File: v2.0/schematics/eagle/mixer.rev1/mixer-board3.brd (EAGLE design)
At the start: 100 x 80 mm, 64 parts, among them IC1 TL082P, IC2 TL082P, IC3 TL082P, IC4 TL082P, J1 RTN-2, J2 RTN-1, J3 SEND1, J4 SEND2

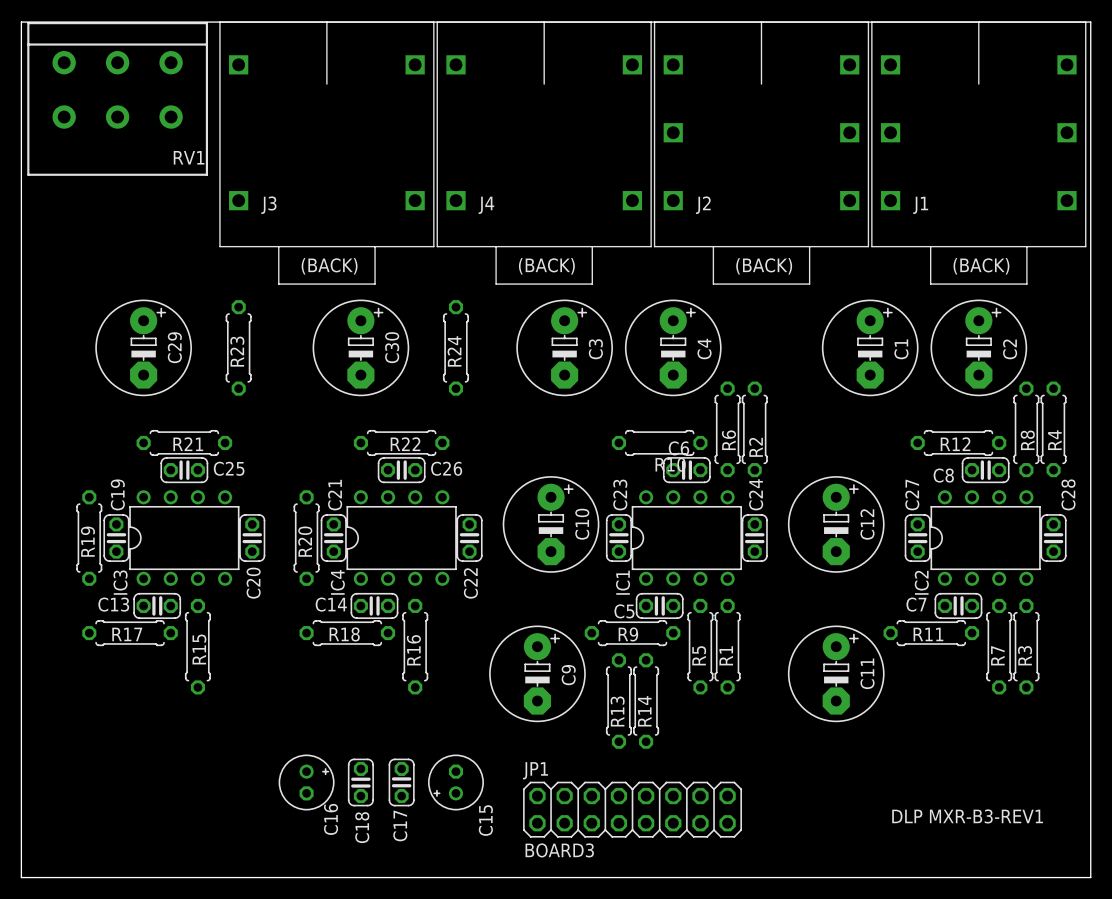
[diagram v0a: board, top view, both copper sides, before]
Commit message: Mixer board 3 route and ground plane
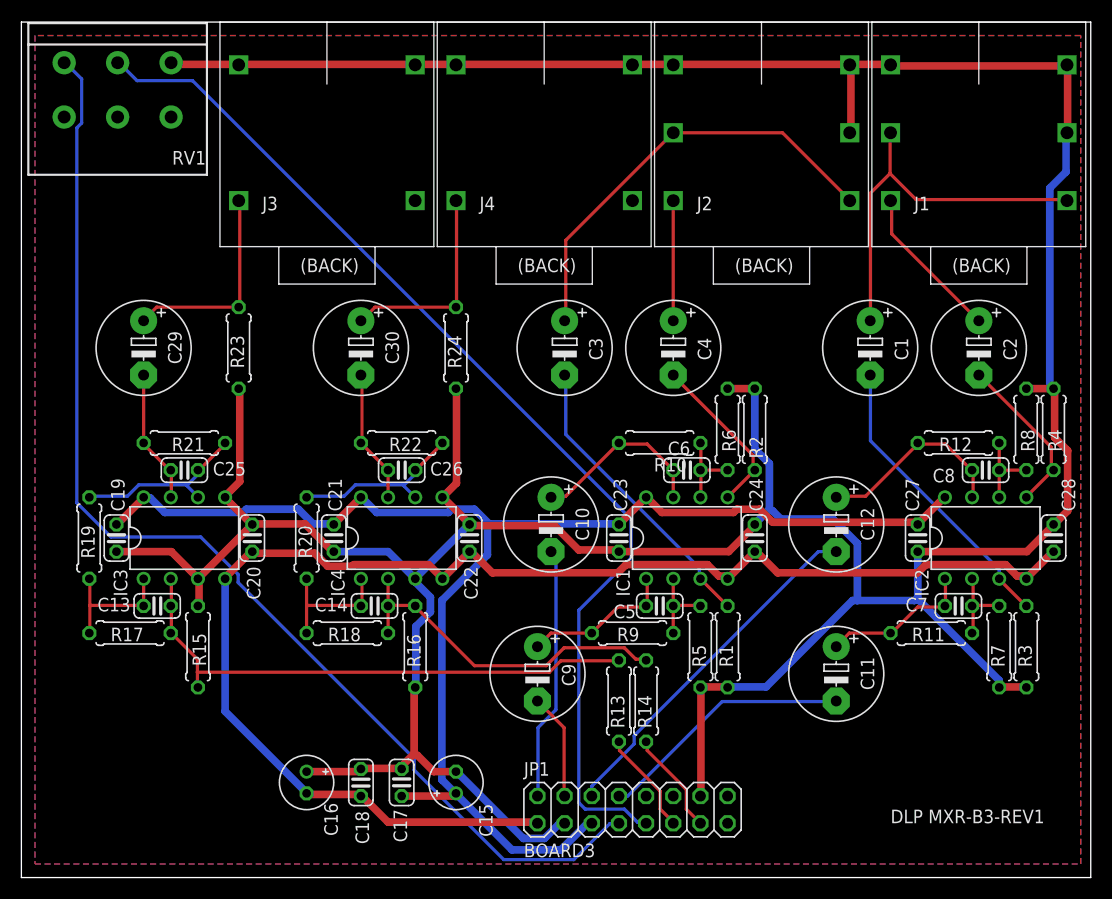
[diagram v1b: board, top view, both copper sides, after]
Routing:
- net 0V: track 0.00 -> 382.6 mm
- net +12V: track 0.00 -> 134.3 mm
- net -12V: track 0.00 -> 132.3 mm
- net M2-LVL-3: track 0.00 -> 109.1 mm
- net M2-LVL-2: track 0.00 -> 101.3 mm
- net N$21: track 0.00 -> 51.2 mm
- net N$1: track 0.00 -> 41.0 mm
- net N$19: track 0.00 -> 36.0 mm
- net RTN2-L: track 0.00 -> 33.3 mm
- net N$25: track 0.00 -> 32.8 mm
- net N$6: track 0.00 -> 27.9 mm
- net N$15: track 0.00 -> 27.7 mm
- net RTN2-R: track 0.00 -> 24.0 mm
- net RTN1-L: track 0.00 -> 23.8 mm
- net OUT-LVL-6: track 0.00 -> 19.6 mm
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- added copper zone on layer 1, net 0V
- added copper zone on layer 16, net 0V

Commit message: Board corrections
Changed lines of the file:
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@@
 <grid distance="50" unitdist="mil" unit="mm" style="lines" multiple="1" display="yes" altdistance="0.635" altunitdist="mm" altunit="mm"/>
 <layers>
-<layer number="1" name="Top" color="4" fill="1" visible="yes" active="yes"/>
-<layer number="16" name="Bottom" color="1" fill="1" visible="yes" active="yes"/>
+<layer number="1" name="Top" color="4" fill="1" visible="no" active="yes"/>
+<layer number="16" name="Bottom" color="1" fill="1" visible="no" active="yes"/>
 <layer number="17" name="Pads" color="2" fill="1" visible="yes" active="yes"/>
 <layer number="18" name="Vias" color="2" fill="1" visible="yes" active="yes"/>
@@
 </element>
 <element name="C6" library="_common" package="C025-024X044" value="22pF" x="62.23" y="38.1" smashed="yes">
-<attribute name="NAME" x="60.452" y="39.497" size="1.27" layer="25" ratio="10"/>
+<attribute name="NAME" x="57.277" y="37.592" size="1.27" layer="25" ratio="10"/>
 <attribute name="VALUE" x="60.452" y="35.433" size="1.27" layer="27" ratio="10"/>
 </element>
@@
 </element>
 <element name="R10" library="_common" package="0207/7" value="30k" x="59.69" y="40.64" smashed="yes" rot="R180">
-<attribute name="NAME" x="62.23" y="39.243" size="1.27" layer="25" ratio="10" rot="R180"/>
+<attribute name="NAME" x="60.96" y="41.148" size="1.27" layer="25" ratio="10" rot="R180"/>
 <attribute name="VALUE" x="61.976" y="41.1988" size="1.27" layer="27" ratio="10" rot="R180"/>
 </element>
@@
 </element>
 <element name="R2" library="_common" package="0207/7" value="10K" x="68.58" y="41.91" smashed="yes" rot="R270">
-<attribute name="NAME" x="68.072" y="41.275" size="1.27" layer="25" ratio="10" rot="R270"/>
+<attribute name="NAME" x="68.072" y="41.91" size="1.27" layer="25" ratio="10" rot="R270"/>
 <attribute name="VALUE" x="68.0212" y="44.196" size="1.27" layer="27" ratio="10" rot="R270"/>
 </element>
